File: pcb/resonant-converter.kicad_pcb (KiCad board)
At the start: 4 copper layers, 100 x 55 mm, 147 parts, among them J1 Banana_Jack_Keystone_575-8, J2 Banana_Jack_Keystone_575-8, J3 Banana_Jack_Keystone_575-8, J4 Banana_Jack_Keystone_575-8, J5 Molex_KK_1x4_0470531000, J6 JST_SH_1x4_BM04B-SRSS-TB-LF-SN, Q1 HSU30N20, Q2 HSU30N20, Q3 MDU04N010VRH, Q4 MDU04N010VRH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

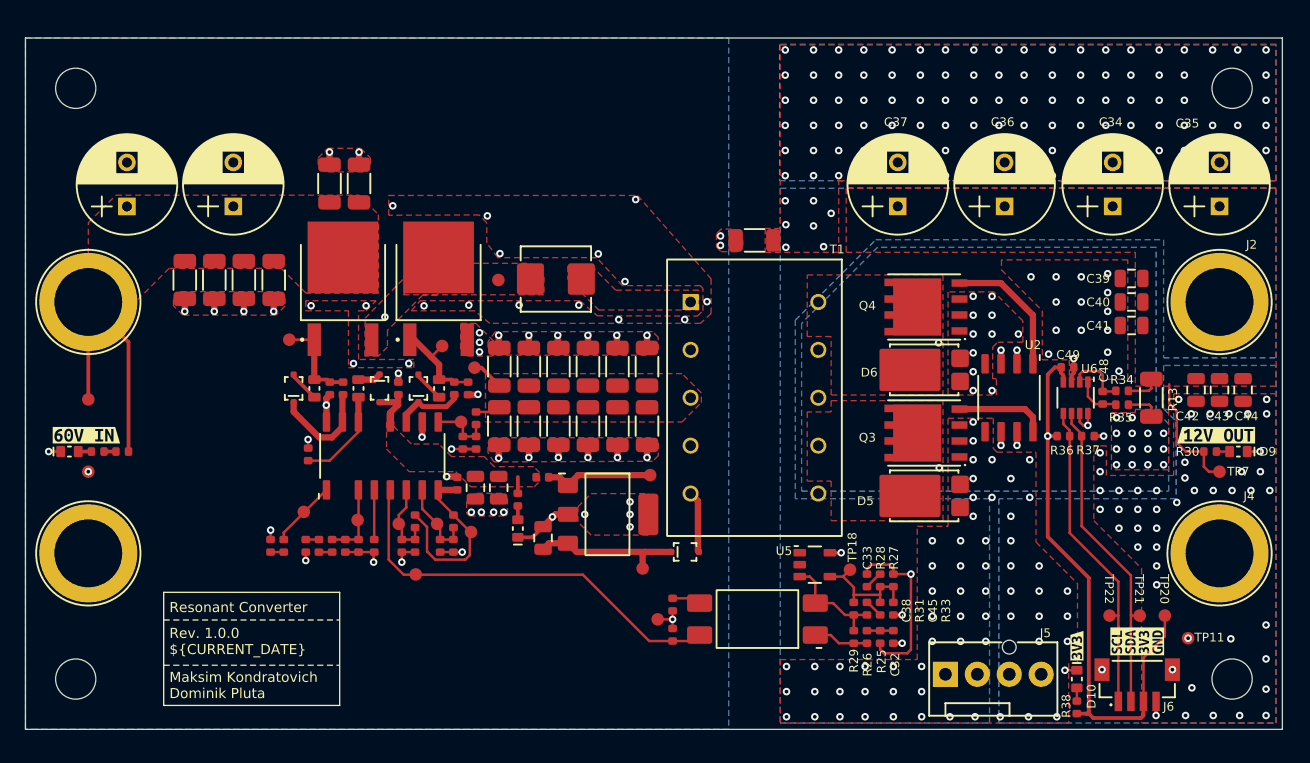
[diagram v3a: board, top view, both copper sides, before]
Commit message: Added via stitching to the primary side
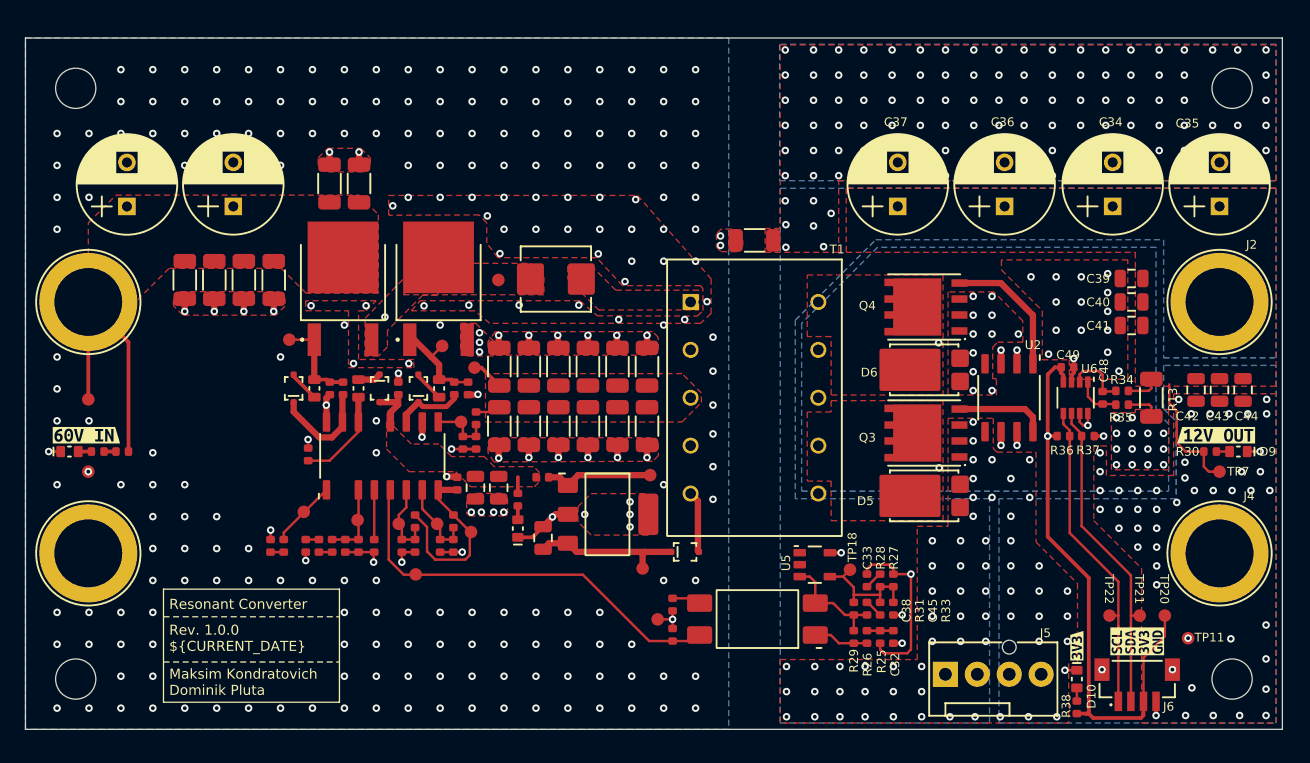
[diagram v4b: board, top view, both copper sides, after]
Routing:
- net GND: vias 54 -> 252
